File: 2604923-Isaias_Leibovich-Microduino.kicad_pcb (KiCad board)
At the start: 2 copper layers, 14 parts, among them J1 USB_A_UCC, J2 Header, U1 ATtiny13-20S

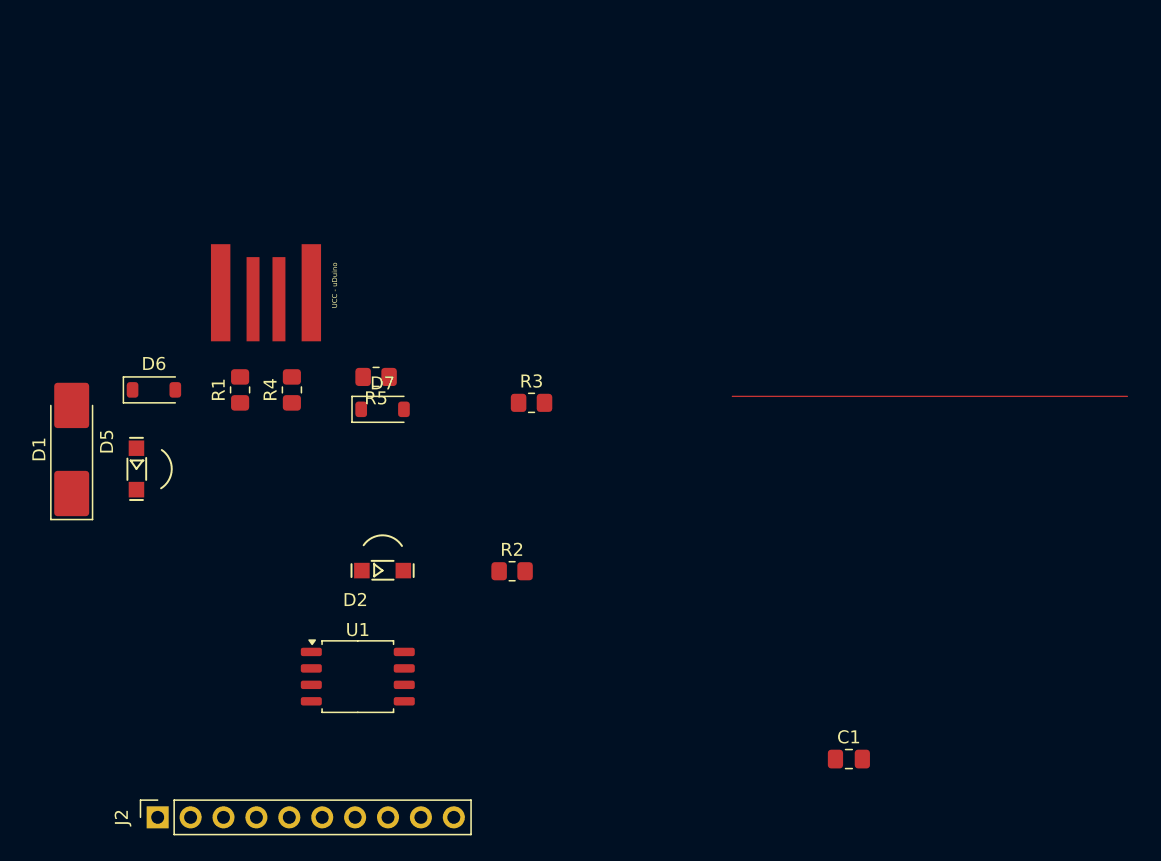
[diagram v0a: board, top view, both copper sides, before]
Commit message: agregue las rutas en el pcb
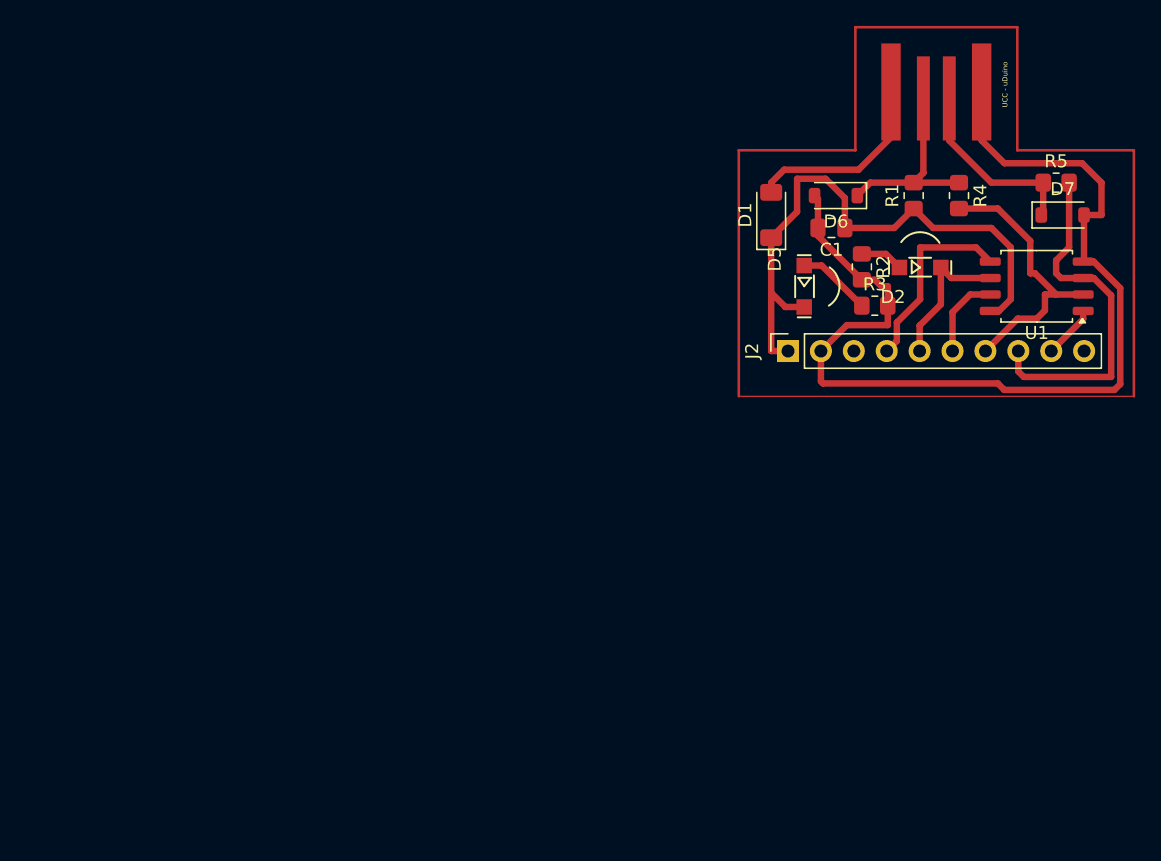
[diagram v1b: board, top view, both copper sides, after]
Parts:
- D1: footprint Diode_SMD:D_MELF_Handsoldering -> Diode_SMD:D_MiniMELF
- moved J2 60.5 mm to (156.8, 85.5)
- moved U1 60.5 mm to (176.0, 80.5), turned to 180 degrees
- moved D1 57.0 mm to (155.5, 75.0)
- moved D6 54.7 mm to (160.5, 73.5), turned to 180 degrees
- moved D7 54.6 mm to (178.0, 75.0)
- moved R5 54.6 mm to (177.5, 72.5), turned to 0 degrees
- moved R1 54.1 mm to (166.5, 73.5)
- moved J1 54.0 mm to (168.2, 65.7)
- moved R4 53.6 mm to (170.0, 73.5), turned to -90 degrees
- moved D5 53.4 mm to (158.5, 81.0)
- moved D2 47.6 mm to (167.5, 78.6)
- moved C1 41.0 mm to (160.2, 76.0), turned to 180 degrees
- moved R2 35.8 mm to (162.5, 79.0), turned to -90 degrees
- moved R3 27.5 mm to (163.5, 82.0)
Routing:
- net GND: track 0.00 -> 78.1 mm
- net +5V: track 0.00 -> 45.7 mm
- net Net-(J2-Pin_8): track 0.00 -> 27.6 mm
- net Net-(J2-Pin_7): track 0.00 -> 21.8 mm
- net Net-(D6-K): track 0.00 -> 15.1 mm
- net Net-(D1-A): track 0.00 -> 14.9 mm
- net Net-(J2-Pin_4): track 0.00 -> 14.9 mm
- net Net-(D7-K): track 0.00 -> 14.4 mm
- net Net-(D2-A): track 0.00 -> 11.3 mm
- net Net-(J2-Pin_6): track 0.00 -> 6.48 mm
- net Net-(D5-K): track 0.00 -> 5.73 mm
- net Net-(J2-Pin_9): track 0.00 -> 4.12 mm
- net Net-(D2-K): track 0.00 -> 3.33 mm
